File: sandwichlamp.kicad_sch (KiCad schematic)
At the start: 21 parts, among them J1 Pole1, J2 Pole2, J3 Pole3, J4 12V Enable, J5 HLK-LD2410C, SW1 Rader Power, SW3 POWER, U1 magnetic-charger, U3 hw357, U4 RX480E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

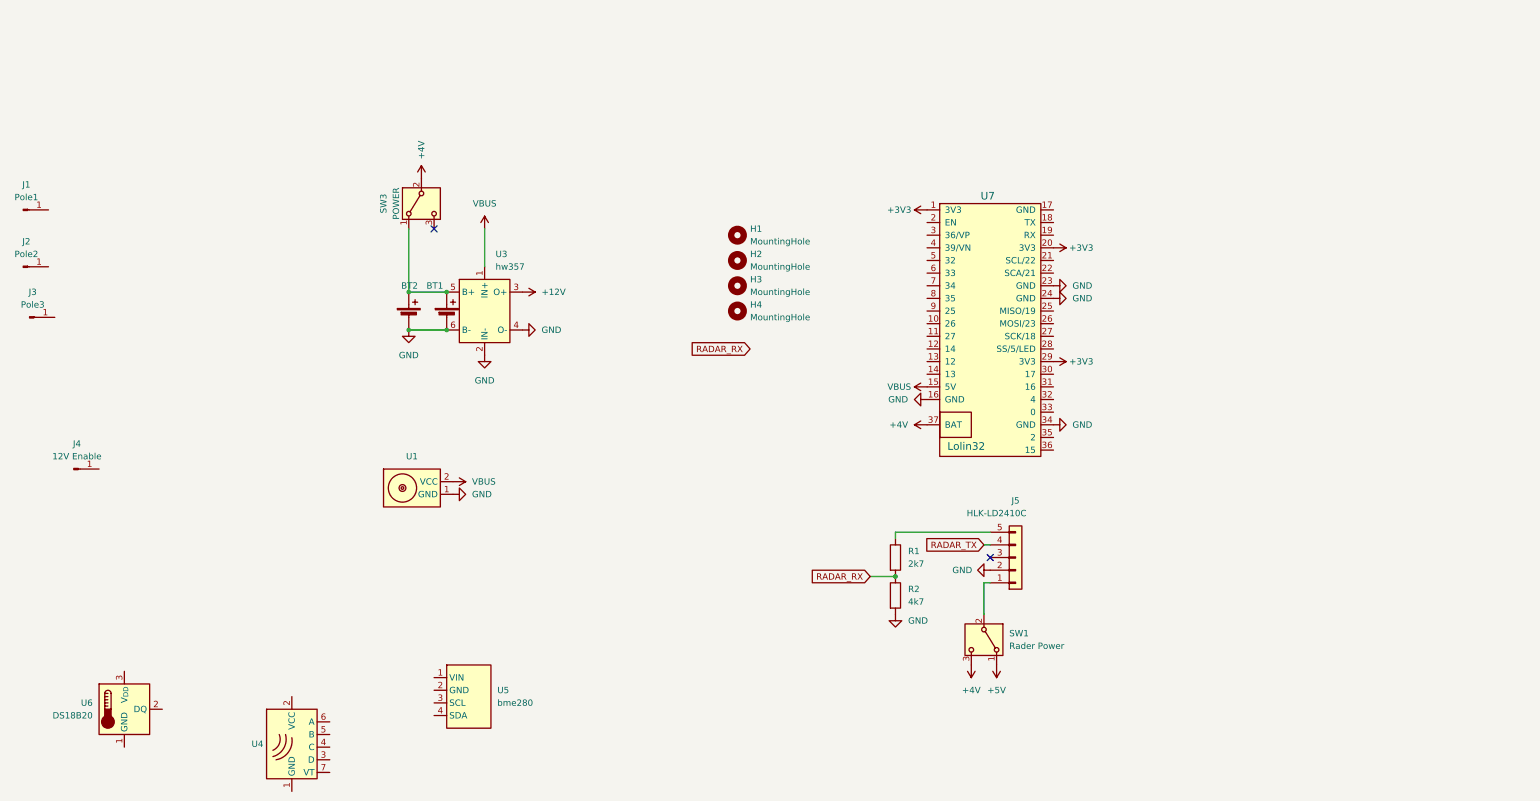
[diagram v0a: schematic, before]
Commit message: Add a light sensor and the labels for the existing components
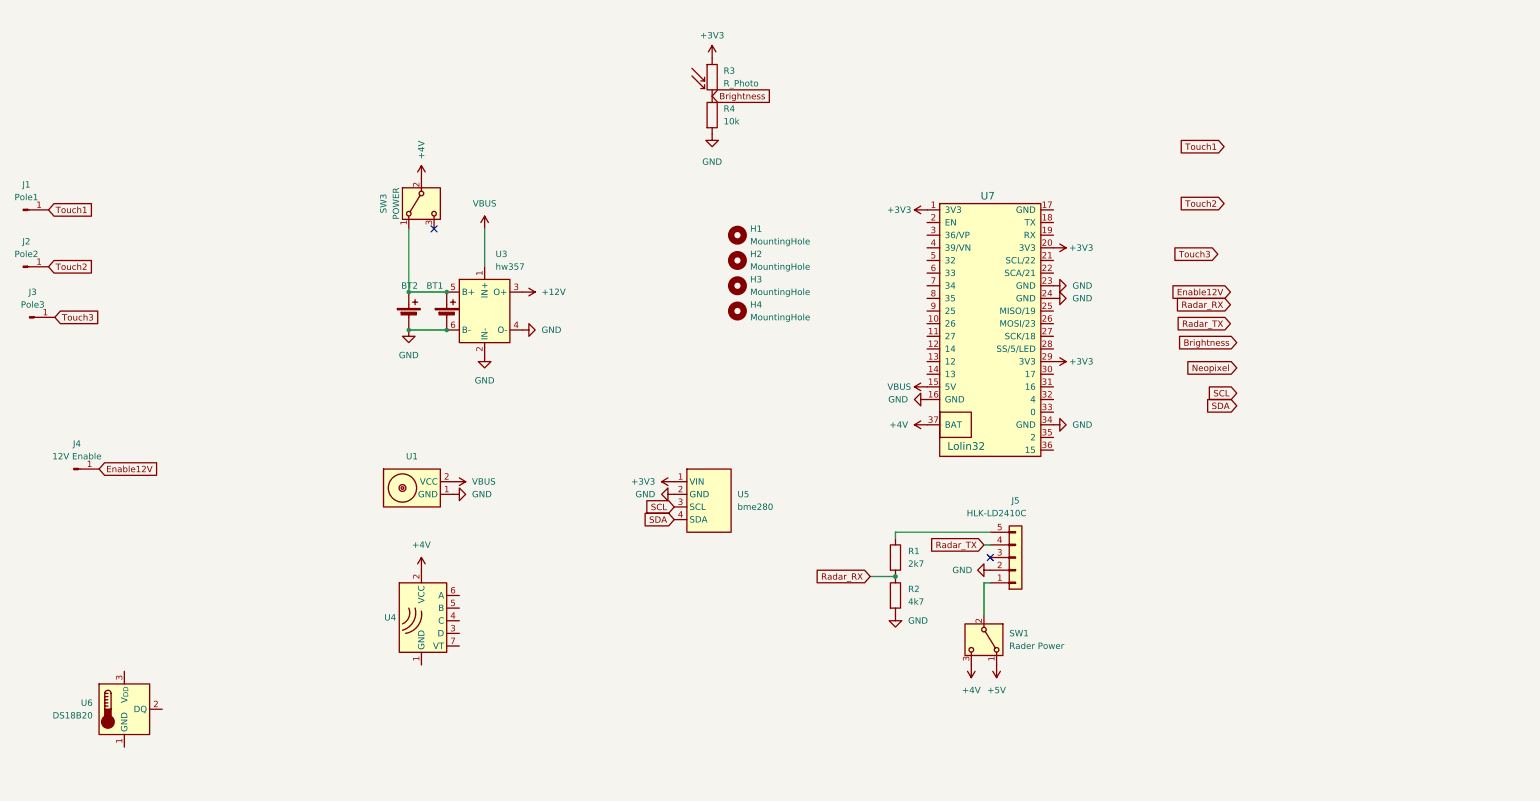
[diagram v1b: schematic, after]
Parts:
- added R3: R_Photo, OptoDevice:R_LDR_5.0x4.1mm_P3mm_Vertical, symbol Device:R_Photo
- added R4: 10k, Resistor_THT:R_Axial_DIN0207_L6.3mm_D2.5mm_P7.62mm_Horizontal, symbol Device:R
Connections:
- net +3V3: now also U5.1 (VIN), R3.1
- net +4V: now also U4.2 (VCC)
- net GND: now also U5.2 (GND), R4.2
- net Touch1: now reaches J1.1 (Pin_1)
- net Touch3: now reaches J3.1 (Pin_1)
- net Enable12V: now reaches J4.1 (Pin_1)
- net Touch2: now reaches J2.1 (Pin_1)
- net SCL: now reaches U5.3 (SCL)
- net SDA: now reaches U5.4 (SDA)
- net RADAR_RX renamed Radar_RX
- net RADAR_TX renamed Radar_TX
- new net Brightness: R3.2, R4.1
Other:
- moved on the sheet: U4, U5

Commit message: Add battery sensing
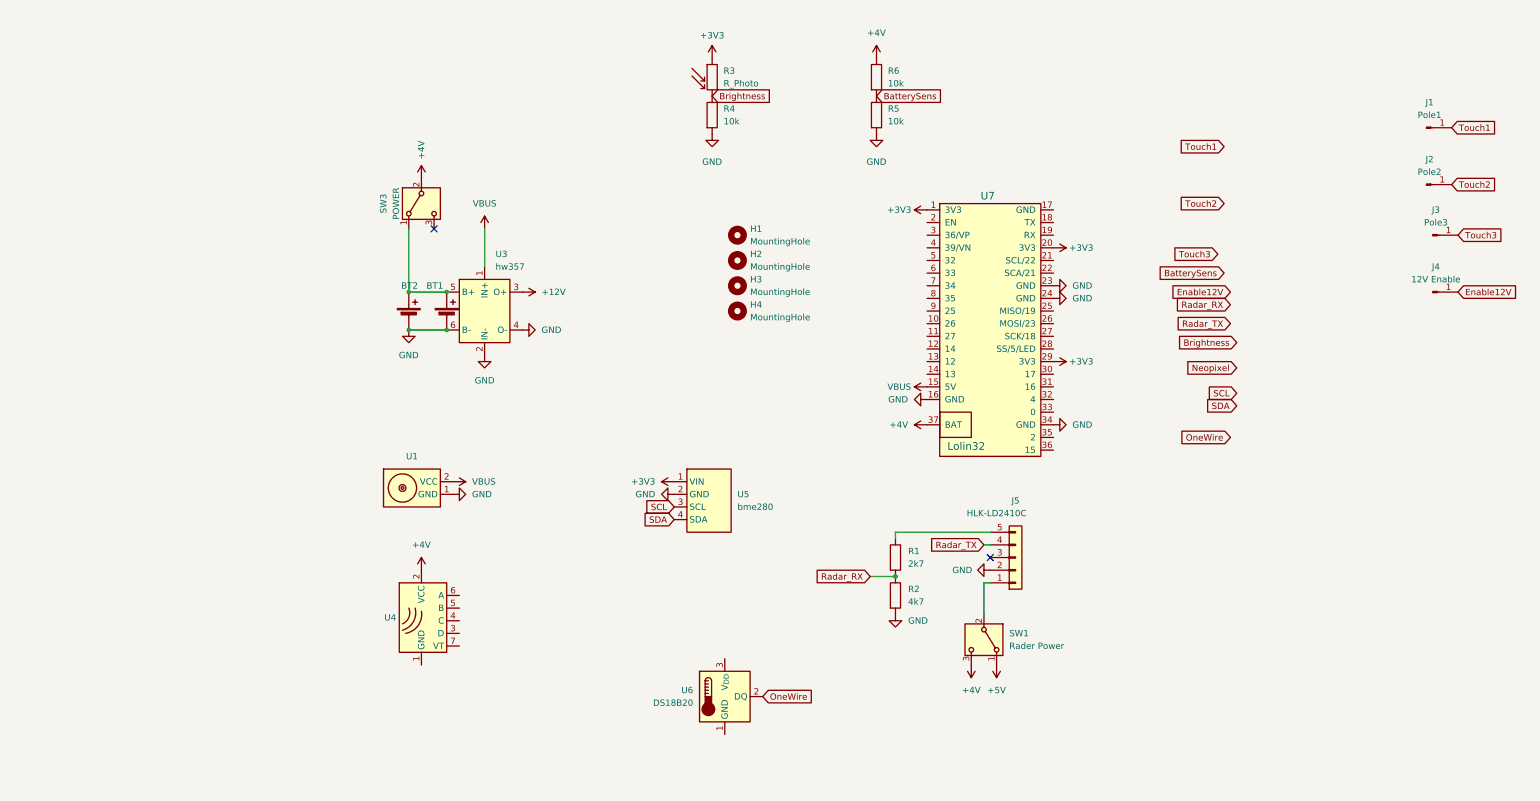
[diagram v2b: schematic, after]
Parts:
- added R5, R6: 10k, Resistor_THT:R_Axial_DIN0207_L6.3mm_D2.5mm_P7.62mm_Horizontal, symbol Device:R
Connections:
- net +4V: now also R6.1
- net GND: now also R5.2
- net OneWire: now reaches U6.2 (DQ)
- new net BatterySens: R5.1, R6.2
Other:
- moved on the sheet: J1, J2, J3, J4, U6

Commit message: Add Neopixel footprint and do the preliminary routing
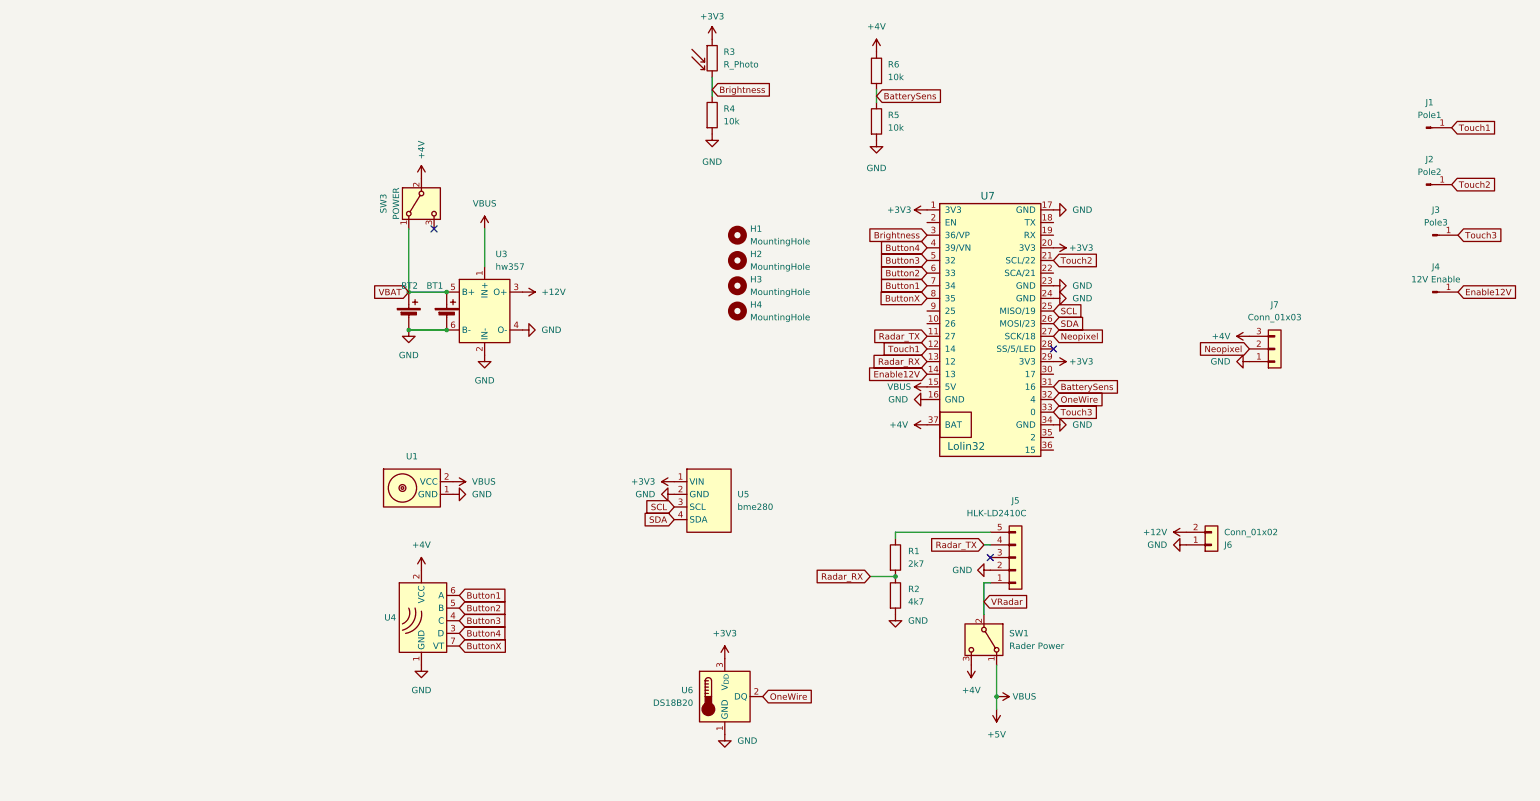
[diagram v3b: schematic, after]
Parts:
- added J6: Conn_01x02, Connector_PinHeader_2.54mm:PinHeader_1x02_P2.54mm_Vertical, symbol Connector_Generic:Conn_01x02
- added J7: Conn_01x03, Connector_PinHeader_2.54mm:PinHeader_1x03_P2.54mm_Vertical, symbol Connector_Generic:Conn_01x03
- R5, R6: footprint Resistor_THT:R_Axial_DIN0207_L6.3mm_D2.5mm_P7.62mm_Horizontal -> Resistor_SMD:R_0805_2012Metric_Pad1.20x1.40mm_HandSolder
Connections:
- net VBUS is gone; now on net +5V: U1.2 (VCC), U3.1 (IN+), U7.15 (5V)
- net +12V: now also J6.2 (Pin_2)
- net +3V3: now also U6.3 (V_{DD})
- net +4V: now also J7.3 (Pin_3)
- net BatterySens: now also U7.31 (16)
- net Brightness: now also U7.3 (36/VP)
- net Enable12V: now also U7.14 (13)
- net GND: now also U4.1 (GND), U6.1 (GND), U7.17 (GND), J6.1 (Pin_1), J7.1 (Pin_1)
- net Neopixel: now also U7.27 (SCK/18), J7.2 (Pin_2)
- net OneWire: now also U7.32 (4)
- net Radar_RX: now also U7.13 (12)
- net Radar_TX: now also U7.11 (27)
- net SCL: now also U7.25 (MISO/19)
- net SDA: now also U7.26 (MOSI/23)
- net Touch1: now also U7.12 (14)
- net Touch2: now also U7.21 (SCL/22)
- net Touch3: now also U7.33 (0)
- net VBAT: now reaches BT1.1 (+), BT2.1 (+), SW3.1 (A), U3.5 (B+)
- net Button4: now reaches U7.4 (39/VN)
- net Button4: now also U4.3 (D)
- net Button3: now reaches U7.5 (32)
- net Button3: now also U4.4 (C)
- net Button2: now reaches U7.6 (33)
- net Button2: now also U4.5 (B)
- net Button1: now reaches U7.7 (34)
- net Button1: now also U4.6 (A)
- net ButtonX: now reaches U7.8 (35)
- net ButtonX: now also U4.7 (VT)
- net VRadar: now reaches J5.1 (Pin_1), SW1.2 (B)
- no-connect marks 2 -> 3
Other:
- moved on the sheet: R3, R5, R6

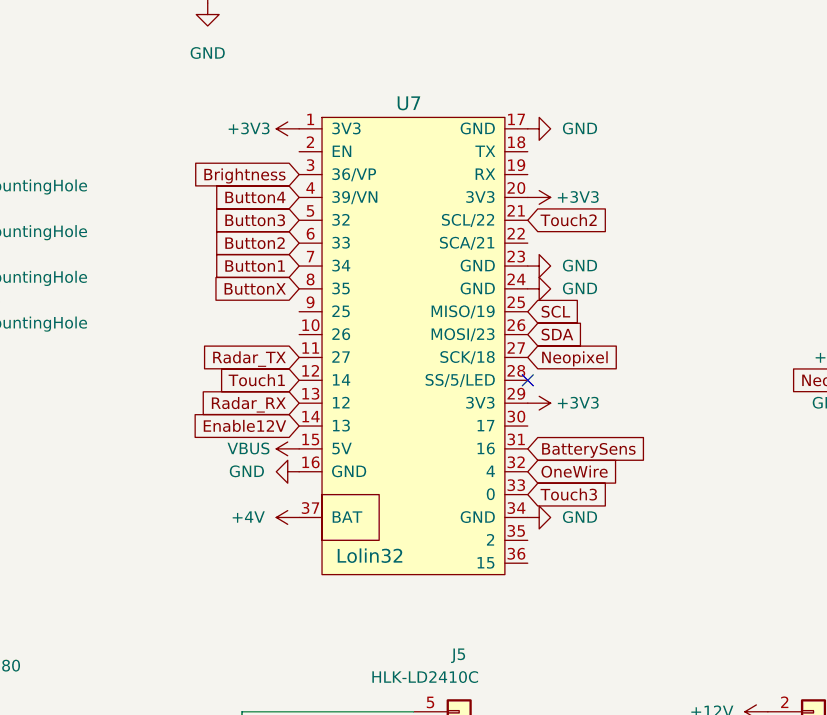
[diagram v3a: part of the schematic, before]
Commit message: Relocate the light sensor so that it can actually sense some light from the top of the lamp
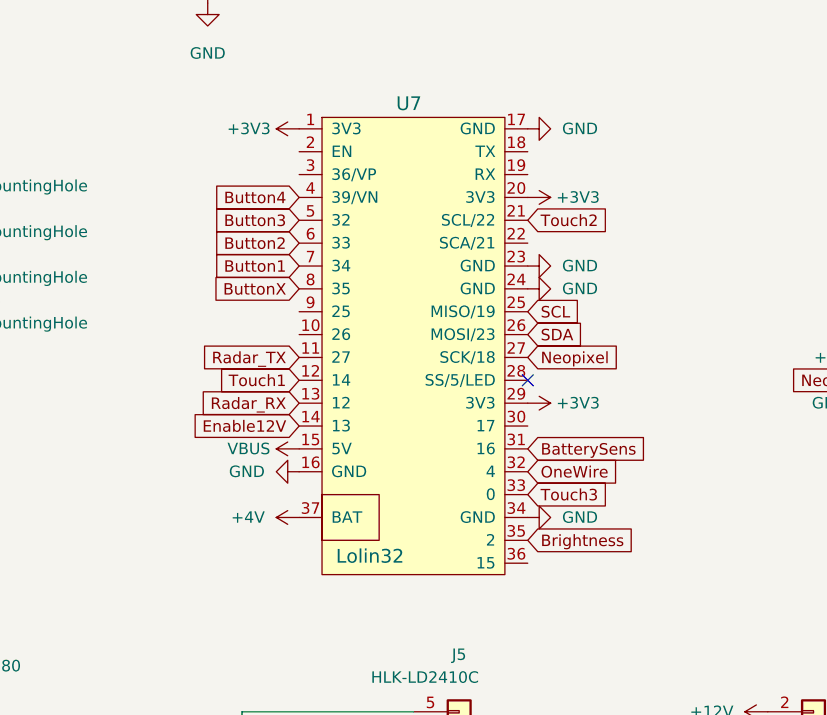
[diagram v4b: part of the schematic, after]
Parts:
- R4: footprint Resistor_THT:R_Axial_DIN0207_L6.3mm_D2.5mm_P7.62mm_Horizontal -> Resistor_SMD:R_0805_2012Metric_Pad1.20x1.40mm_HandSolder
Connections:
- net Brightness: now also U7.35 (2); no longer U7.3 (36/VP)
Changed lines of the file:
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@@
 	(global_label "Brightness"
 		(shape input)
-		(at 130.81 62.23 180)
-		(fields_autoplaced yes)
-		(effects
-			(font
-				(size 1.27 1.27)
-			)
-			(justify right)
-		)
-		(property "Intersheetrefs" "${INTERSHEET_REFS}"
-			(at 117.8463 62.23 0)
-			(effects
-				(font
-					(size 1.27 1.27)
-				)
-				(justify right)
+		(at 156.21 102.87 0)
+		(fields_autoplaced yes)
+		(effects
+			(font
+				(size 1.27 1.27)
+			)
+			(justify left)
+		)
+		(property "Intersheetrefs" "${INTERSHEET_REFS}"
+			(at 169.1737 102.87 0)
+			(effects
+				(font
+					(size 1.27 1.27)
+				)
+				(justify left)
 				(hide yes)
 			)
@@
 			)
 		)
-		(property "Footprint" "Resistor_THT:R_Axial_DIN0207_L6.3mm_D2.5mm_P7.62mm_Horizontal"
+		(property "Footprint" "Resistor_SMD:R_0805_2012Metric_Pad1.20x1.40mm_HandSolder"
 			(at 85.852 38.1 90)
 			(effects

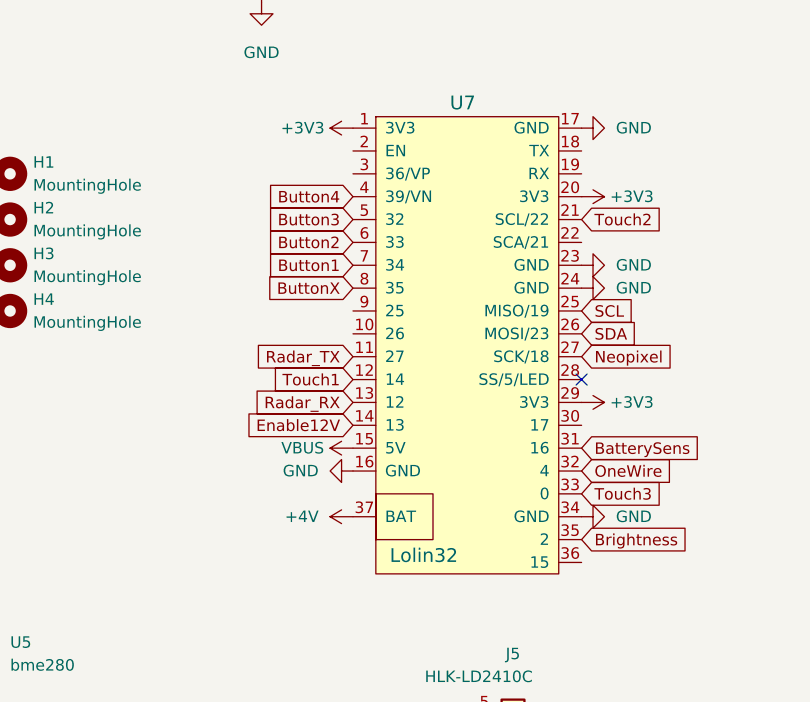
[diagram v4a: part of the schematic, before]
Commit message: Make sure input-only pins are used as such
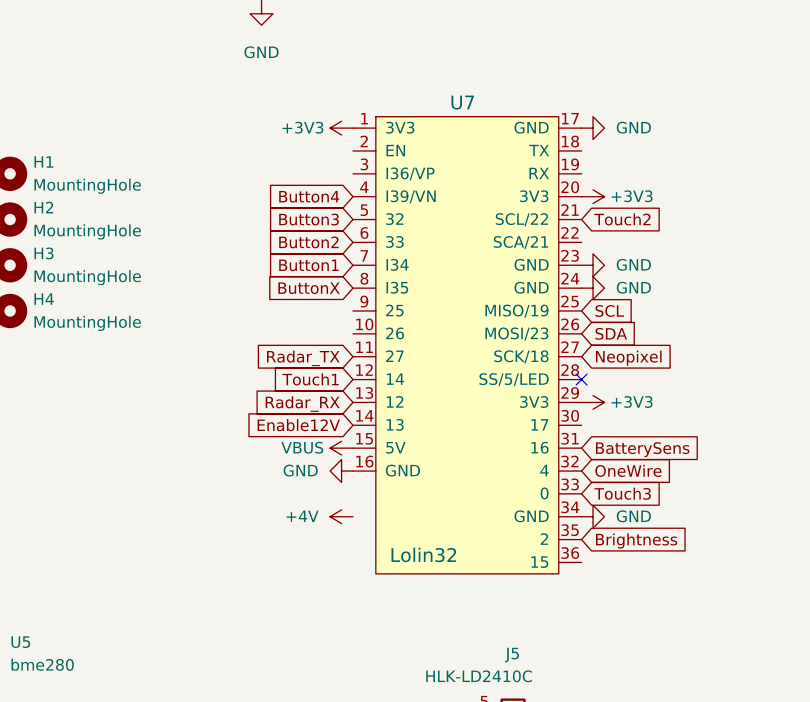
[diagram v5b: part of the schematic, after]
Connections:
- net +4V: no longer U7.37 (BAT)
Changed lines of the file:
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@@
 		(pin "25"
-		)
-		(pin "37"
 		)
 		(instances

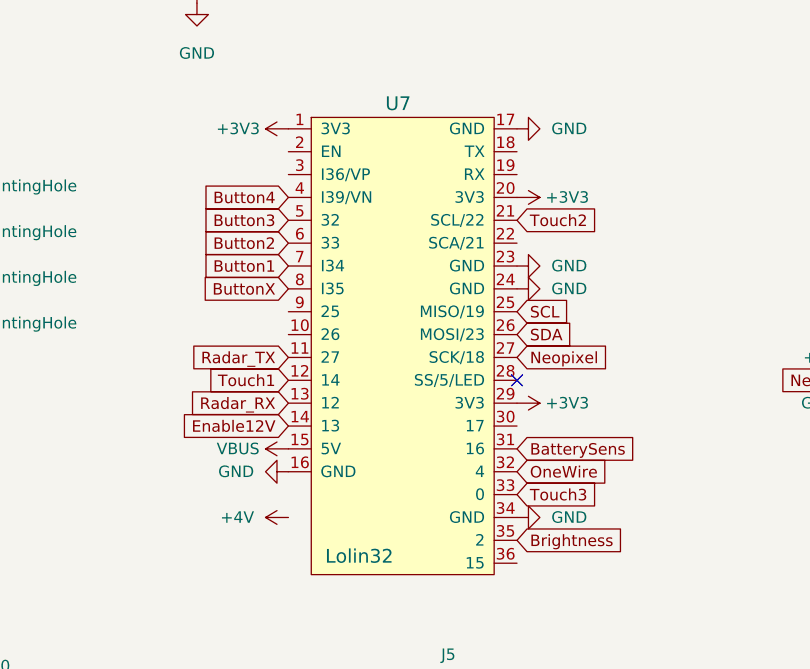
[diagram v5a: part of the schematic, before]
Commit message: Fix the touch buttons
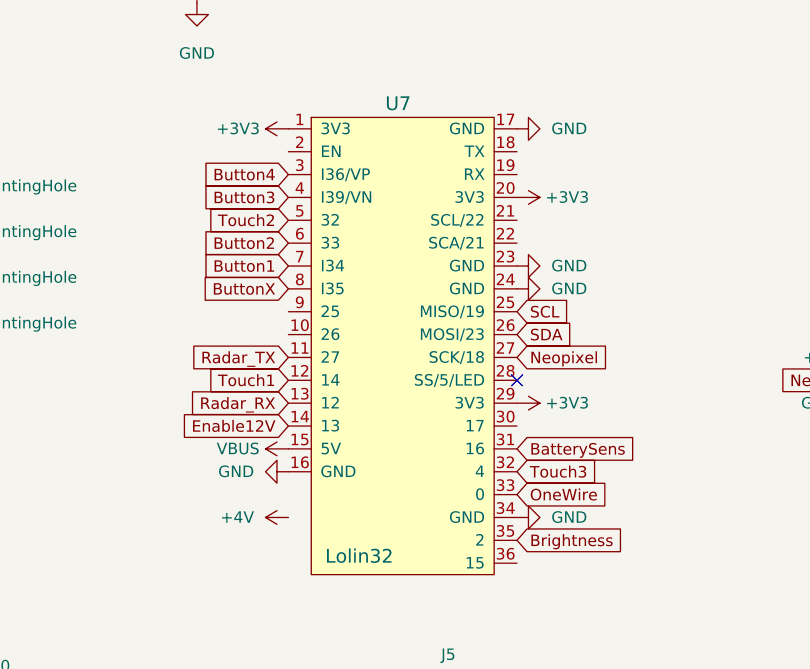
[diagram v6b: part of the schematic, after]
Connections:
- net Button3: now also U7.4 (I39/VN); no longer U7.5 (32)
- net Button4: now also U7.3 (I36/VP); no longer U7.4 (I39/VN)
- net OneWire: now also U7.33 (0); no longer U7.32 (4)
- net Touch2: now also U7.5 (32); no longer U7.21 (SCL/22)
- net Touch3: now also U7.32 (4); no longer U7.33 (0)
